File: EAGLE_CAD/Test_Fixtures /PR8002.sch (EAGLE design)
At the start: 54 parts, among them J1 M3_SCREW_POST

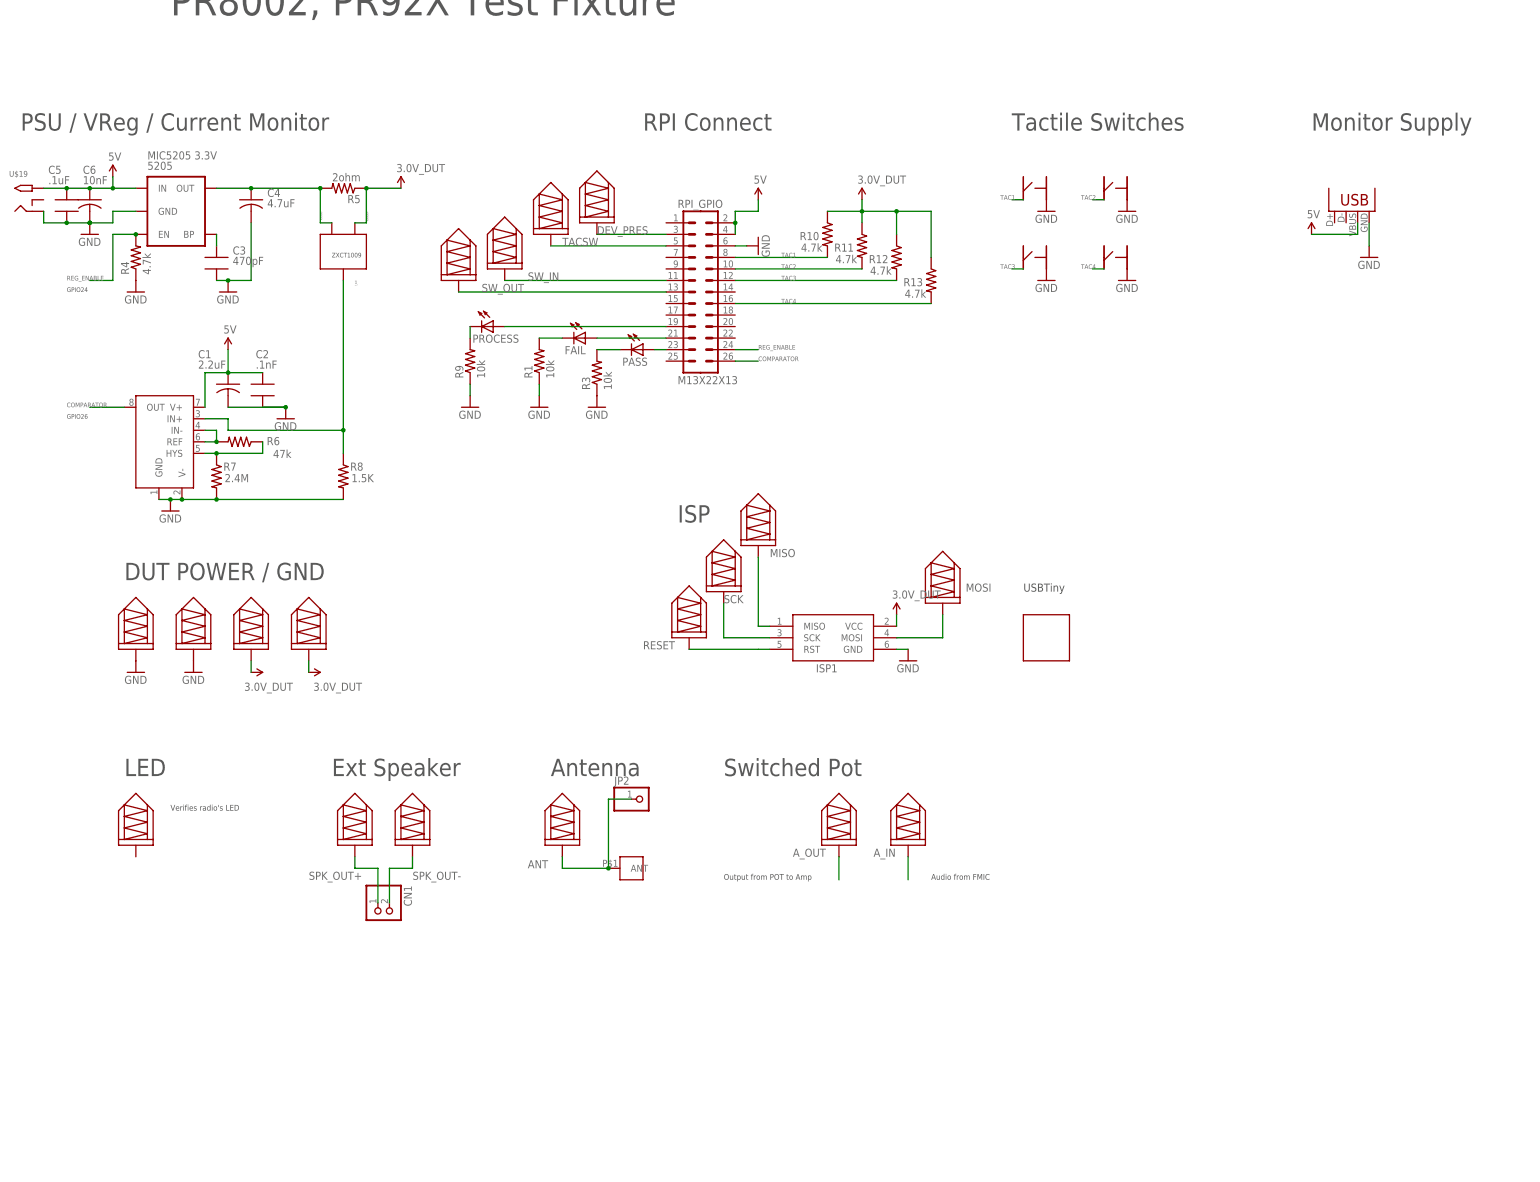
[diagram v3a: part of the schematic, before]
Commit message: PR8002 Updates
Placed 26 pin header for RPIB+ as well as Andy’s other comments:
1. Tac1-4 pull up resistors need to go to +3V3 from the RPi, not
3.0V_DUT.
2. I think R1, R3 R9 are all way too high value - I would expect 470R -
1K
3. I suggest putting a trimmer down across A_OUT/A_IN/GND to facilitate
the testing of SMT-only boards, that way the operator can pick the
level that works for the line.
4. SW_IN/SW_OUT should not go to GPIO, they should simple go to two
ends of a zero ohm resistor.
5. The trimmer and the zero ohm resistor used in (3) & (4) would be
depopulated in testers destined for fully assembled boards.
6. Add a 4K7 pullup to 3V3 (pin 1) on DEV_PRES
7. The RPi B+ has a 40 pin header, not the 26 pin one you show.
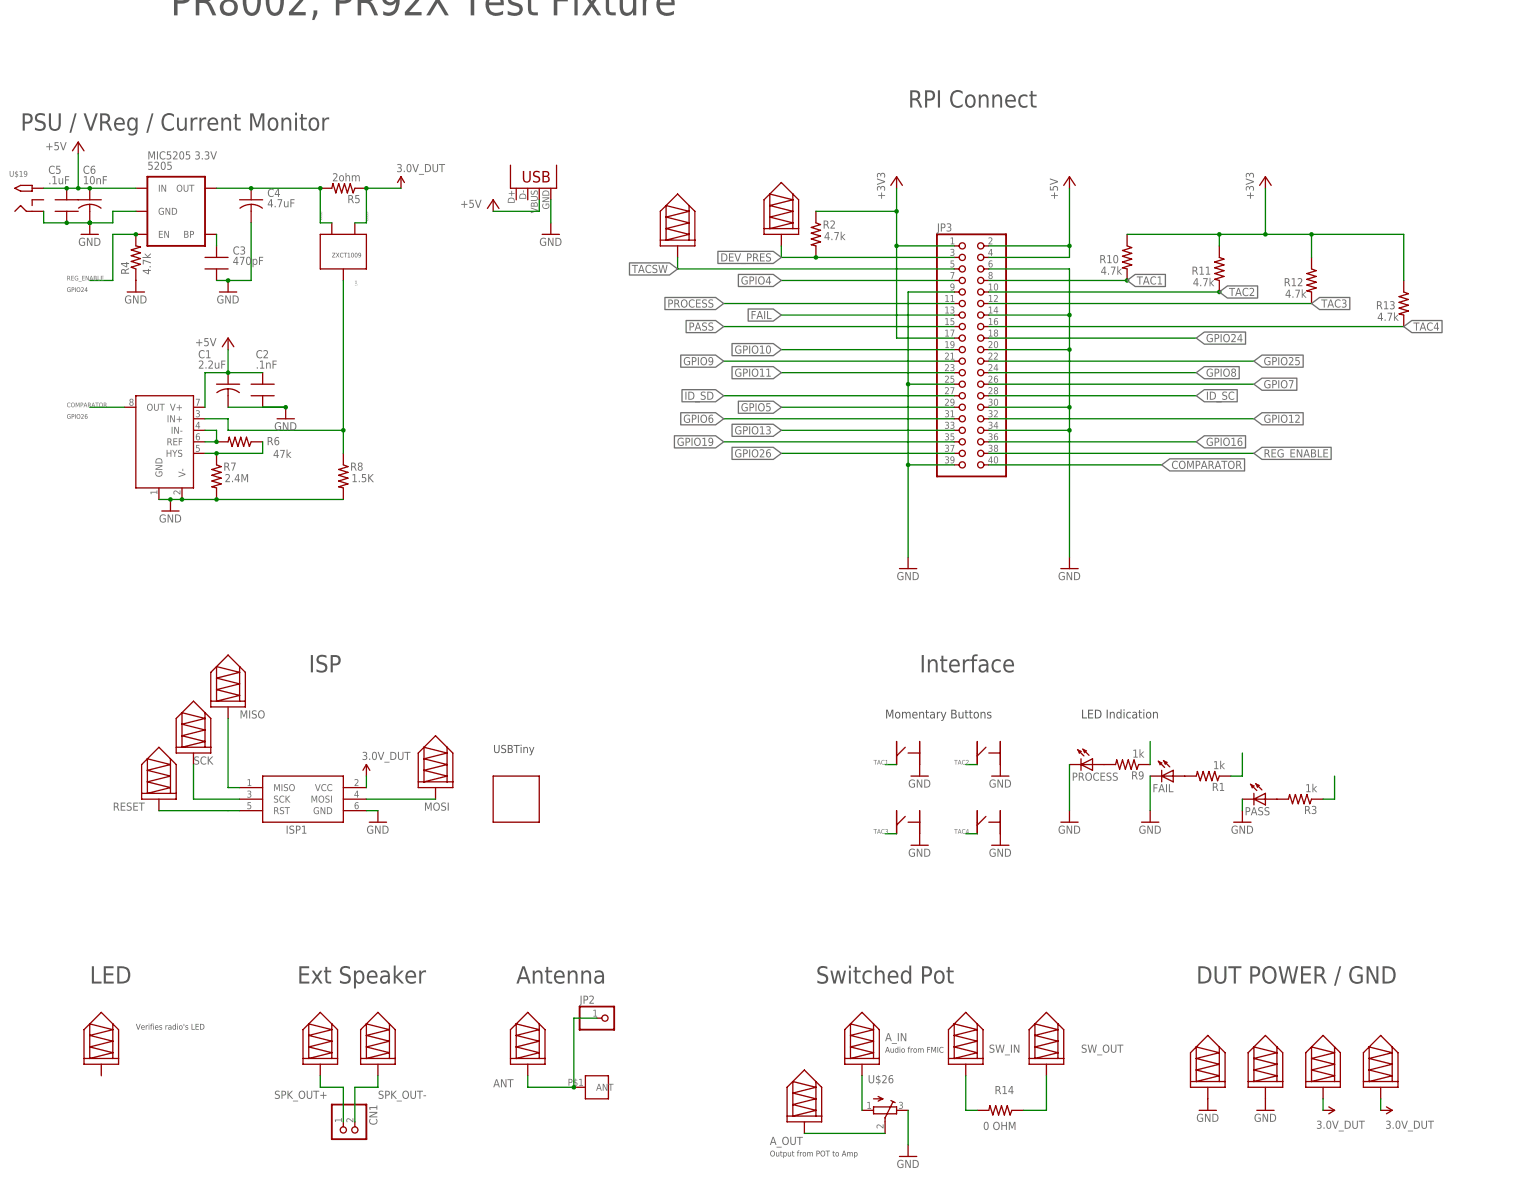
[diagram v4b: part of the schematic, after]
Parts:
- removed RPI_GPIO: M13X22X13, PR_Parts_Library:M13X22X13
- added JP3: (no value), pinhead:PINHD-2X20
- added R14: 0 OHM, PR_Parts_Library:R_SMT_0805_ADAFRUIT
- added R2: 4.7k, PR_Parts_Library:R_SMT_0805_ADAFRUIT
- added U$26: (no value), adafruit:TRIMPOTTC33X
- R1, R3, R9: value 10k -> 1k
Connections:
- removed net 5V: 5205.IN, C1.1, C2.1, C5.1, C6.1, JP1.VBUS, RPI_GPIO.5V, RPI_GPIO.DNC1, TSM931.V+, U$19.TIP
- removed net N$10: PASS.C, R3.2
- removed net N$16: PROCESS.A, RPI_GPIO.GPIO19
- removed net N$17: PROCESS.C, R9.2
- removed net N$7: FAIL.A, RPI_GPIO.GPIO21
- removed net N$8: PASS.A, RPI_GPIO.GPIO23
- removed net N$9: FAIL.C, R1.2
- new net +3V3: JP3.1, JP3.17, R10.1, R11.1, R12.1, R13.1, R2.1
- new net +5V: 5205.IN, C1.1, C2.1, C5.1, C6.1, JP1.VBUS, JP3.2, JP3.4, TSM931.V+, U$19.TIP
- new net FAIL: JP3.13, R1.1
- new net GPIO10: JP3.19
- new net GPIO11: JP3.23
- new net GPIO12: JP3.32
- new net GPIO13: JP3.33
- new net GPIO16: JP3.36
- new net GPIO19: JP3.35
- new net GPIO24: JP3.18
- new net GPIO25: JP3.22
- new net GPIO26: JP3.37
- new net GPIO4: JP3.7
- new net GPIO5: JP3.29
- new net GPIO6: JP3.31
- new net GPIO7: JP3.26
- new net GPIO8: JP3.24
- new net GPIO9: JP3.21
- new net ID_SC: JP3.28
- new net ID_SD: JP3.27
- new net N$2: PROCESS.A, R9.2
- new net N$3: FAIL.A, R1.2
- new net N$4: PASS.A, R3.2
- new net PASS: JP3.15, R3.1
- new net PROCESS: JP3.11, R9.1
- net 3.3V: no longer R10.1, R11.1, R12.1, R13.1
- net A_IN: now also U$26.A
- net A_OUT: now also U$26.S
- net COMPARATOR: now also JP3.40; no longer RPI_GPIO.GPIO26
- net DEV_PRES: now also JP3.3, R2.2; no longer RPI_GPIO.GPIO3
- net GND: now also FAIL.C, JP3.14, JP3.20, JP3.25, JP3.30, JP3.34, JP3.39, JP3.6, JP3.9, PASS.C, PROCESS.C, U$26.E; no longer R1.1, R3.1, R9.1, RPI_GPIO.GND
- net REG_ENABLE: now also JP3.38; no longer RPI_GPIO.GPIO24
- net SW_IN: now also R14.2; no longer RPI_GPIO.GPIO11
- net SW_OUT: now also R14.1; no longer RPI_GPIO.GPIO13
- net TAC1: now also JP3.8; no longer RPI_GPIO.GPIO8
- net TAC2: now also JP3.10; no longer RPI_GPIO.GPIO10
- net TAC3: now also JP3.12; no longer RPI_GPIO.GPIO12
- net TAC4: now also JP3.16; no longer RPI_GPIO.GPIO16
- net TACSW: now also JP3.5; no longer RPI_GPIO.GPIO5
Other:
- note added: "Interface"
- note added: "LED Indication"
- note added: "Momentary Buttons"
- note removed: "Monitor Supply"
- note removed: "Tactile Switches"
- moved on the sheet: CN1, FAIL, ISP1, JP2, PASS, PROCESS, R1, R10, R11, R12, R13, R3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

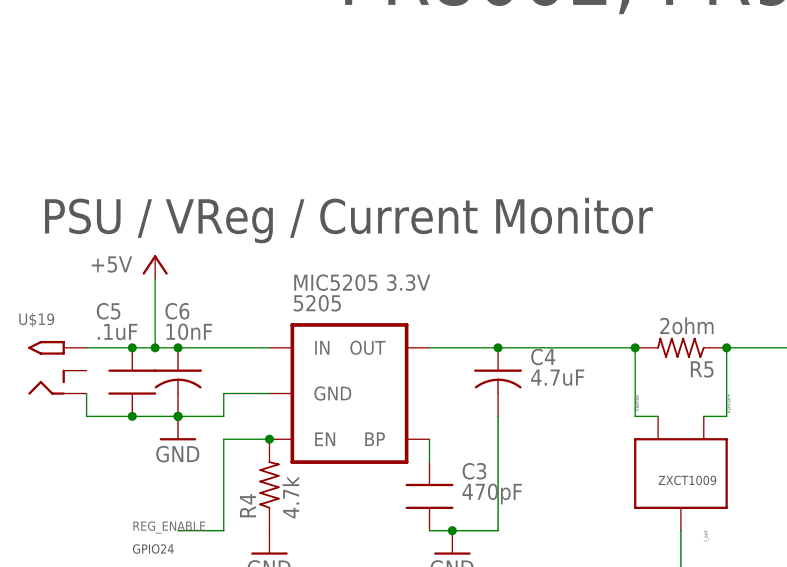
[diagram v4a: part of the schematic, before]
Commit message: Updates PR8002
updated footprint for IDI R-1 receptacle
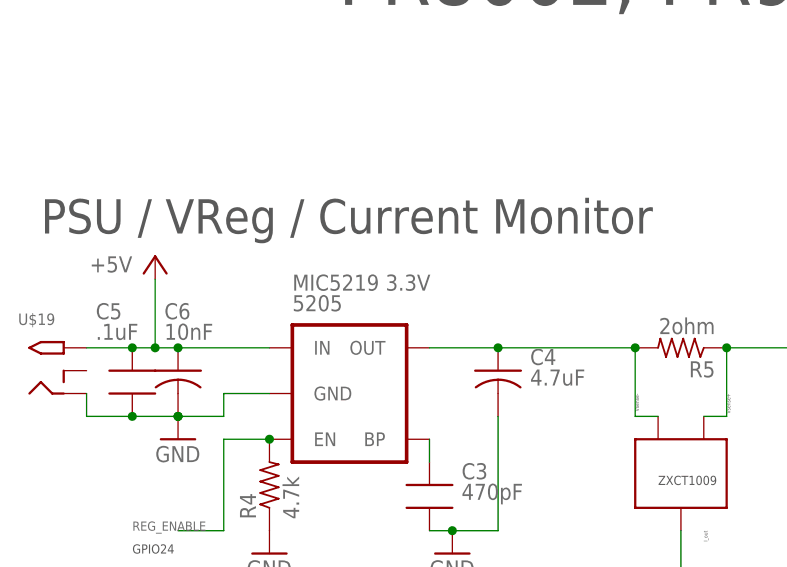
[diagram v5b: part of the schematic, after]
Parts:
- 5205: value MIC5205 3.3V -> MIC5219 3.3V
- U$10, U$11, U$12, U$13, U$14, U$15, U$16, U$17, U$18, U$2, U$21, U$3, U$4, U$5, U$6, U$7, U$8, U$9: value 0908MILL_MAX_SPRINGPIN -> IDI-R2; device PR_Parts_Library:0908MILL_MAX_SPRINGPIN -> PR_Parts_Library:IDI-R2
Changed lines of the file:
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@@
 <?xml version="1.0" encoding="utf-8"?>
 <!DOCTYPE eagle SYSTEM "eagle.dtd">
-<eagle version="7.2.0">
+<eagle version="6.6.0">
 <drawing>
 <settings>
@@
 </classes>
 <parts>
-<part name="U$2" library="PR_Parts_Library" deviceset="0908MILL_MAX_SPRINGPIN" device=""/>
-<part name="U$3" library="PR_Parts_Library" deviceset="0908MILL_MAX_SPRINGPIN" device=""/>
-<part name="U$4" library="PR_Parts_Library" deviceset="0908MILL_MAX_SPRINGPIN" device=""/>
-<part name="U$5" library="PR_Parts_Library" deviceset="0908MILL_MAX_SPRINGPIN" device=""/>
-<part name="U$6" library="PR_Parts_Library" deviceset="0908MILL_MAX_SPRINGPIN" device=""/>
-<part name="U$7" library="PR_Parts_Library" deviceset="0908MILL_MAX_SPRINGPIN" device=""/>
-<part name="U$8" library="PR_Parts_Library" deviceset="0908MILL_MAX_SPRINGPIN" device=""/>
-<part name="U$9" library="PR_Parts_Library" deviceset="0908MILL_MAX_SPRINGPIN" device=""/>
-<part name="U$10" library="PR_Parts_Library" deviceset="0908MILL_MAX_SPRINGPIN" device=""/>
-<part name="U$11" library="PR_Parts_Library" deviceset="0908MILL_MAX_SPRINGPIN" device=""/>
-<part name="U$12" library="PR_Parts_Library" deviceset="0908MILL_MAX_SPRINGPIN" device=""/>
-<part name="U$13" library="PR_Parts_Library" deviceset="0908MILL_MAX_SPRINGPIN" device=""/>
-<part name="U$14" library="PR_Parts_Library" deviceset="0908MILL_MAX_SPRINGPIN" device=""/>
-<part name="U$15" library="PR_Parts_Library" deviceset="0908MILL_MAX_SPRINGPIN" device=""/>
-<part name="U$16" library="PR_Parts_Library" deviceset="0908MILL_MAX_SPRINGPIN" device=""/>
-<part name="U$17" library="PR_Parts_Library" deviceset="0908MILL_MAX_SPRINGPIN" device=""/>
-<part name="U$18" library="PR_Parts_Library" deviceset="0908MILL_MAX_SPRINGPIN" device=""/>
+<part name="U$2" library="PR_Parts_Library" deviceset="IDI-R2" device=""/>
+<part name="U$3" library="PR_Parts_Library" deviceset="IDI-R2" device=""/>
+<part name="U$4" library="PR_Parts_Library" deviceset="IDI-R2" device=""/>
+<part name="U$5" library="PR_Parts_Library" deviceset="IDI-R2" device=""/>
+<part name="U$6" library="PR_Parts_Library" deviceset="IDI-R2" device=""/>
+<part name="U$7" library="PR_Parts_Library" deviceset="IDI-R2" device=""/>
+<part name="U$8" library="PR_Parts_Library" deviceset="IDI-R2" device=""/>
+<part name="U$9" library="PR_Parts_Library" deviceset="IDI-R2" device=""/>
+<part name="U$10" library="PR_Parts_Library" deviceset="IDI-R2" device=""/>
+<part name="U$11" library="PR_Parts_Library" deviceset="IDI-R2" device=""/>
+<part name="U$12" library="PR_Parts_Library" deviceset="IDI-R2" device=""/>
+<part name="U$13" library="PR_Parts_Library" deviceset="IDI-R2" device=""/>
+<part name="U$14" library="PR_Parts_Library" deviceset="IDI-R2" device=""/>
+<part name="U$15" library="PR_Parts_Library" deviceset="IDI-R2" device=""/>
+<part name="U$16" library="PR_Parts_Library" deviceset="IDI-R2" device=""/>
+<part name="U$17" library="PR_Parts_Library" deviceset="IDI-R2" device=""/>
+<part name="U$18" library="PR_Parts_Library" deviceset="IDI-R2" device=""/>
 <part name="U$19" library="adafruit" deviceset="2.1MMJACK" device="THM"/>
 <part name="ISP1" library="adafruit" deviceset="AVRISP" device="-6"/>
 <part name="GND4" library="SparkFun-Aesthetics" deviceset="GND" device=""/>
 <part name="GND6" library="SparkFun-Aesthetics" deviceset="GND" device=""/>
-<part name="U$21" library="PR_Parts_Library" deviceset="0908MILL_MAX_SPRINGPIN" device=""/>
+<part name="U$21" library="PR_Parts_Library" deviceset="IDI-R2" device=""/>
 <part name="CN1" library="PR_Parts_Library" deviceset="JST_2PIN" device="-SMT-RA"/>
 <part name="GND2" library="SparkFun-Aesthetics" deviceset="GND" device=""/>
@@
 <part name="GND11" library="SparkFun-Aesthetics" deviceset="GND" device=""/>
 <part name="GND12" library="SparkFun-Aesthetics" deviceset="GND" device=""/>
-<part name="5205" library="SparkFun-PowerIC" deviceset="V_REG_MIC5219" device="3.3V" value="MIC5205 3.3V">
+<part name="5205" library="SparkFun-PowerIC" deviceset="V_REG_MIC5219" device="3.3V" value="MIC5219 3.3V">
 <attribute name="PROD_ID" value="VREG-5205-3.0"/>
 </part>
